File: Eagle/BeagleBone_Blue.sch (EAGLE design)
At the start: 294 parts, among them M1 JST_ZH_2, M2 JST_ZH_2, M3 JST_ZH_2, M4 JST_ZH_2, P10 SCHA5B0200, Q3 MOSFET-N, U1 TPD4S012_DRY_6, U4 TPD4S012_DRY_6, U5 24LC_32AT-I/OT, U6 SN74LVC1G07_DCK_5, U7 TPS2051B_D_8, U8 MTFC4GLDEA, Y1 CM200C-32.768KAZF-UT, Y2 445C33D24M00000

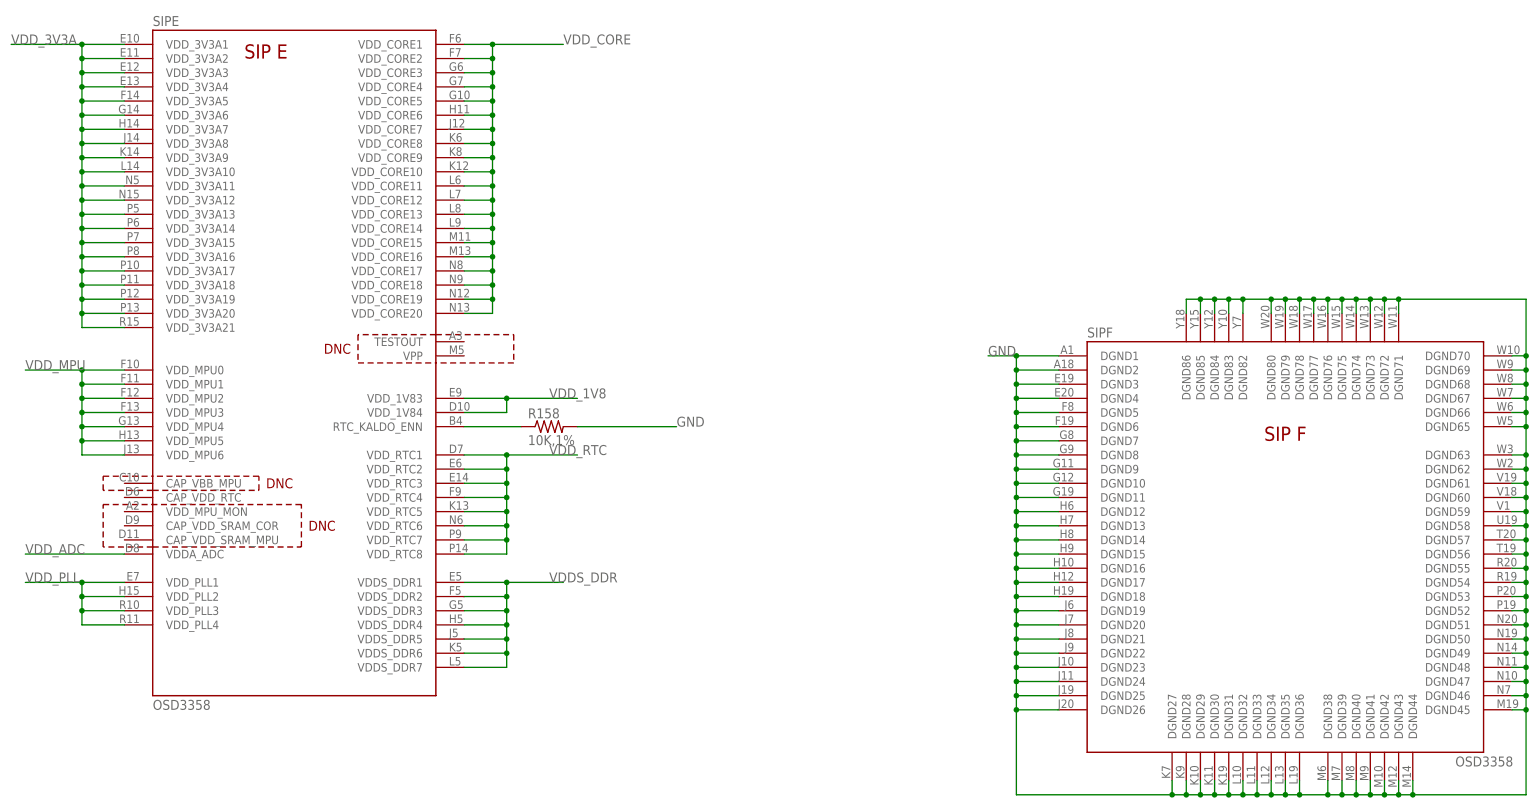
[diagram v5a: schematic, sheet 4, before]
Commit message: Remove extraneous voltage connections
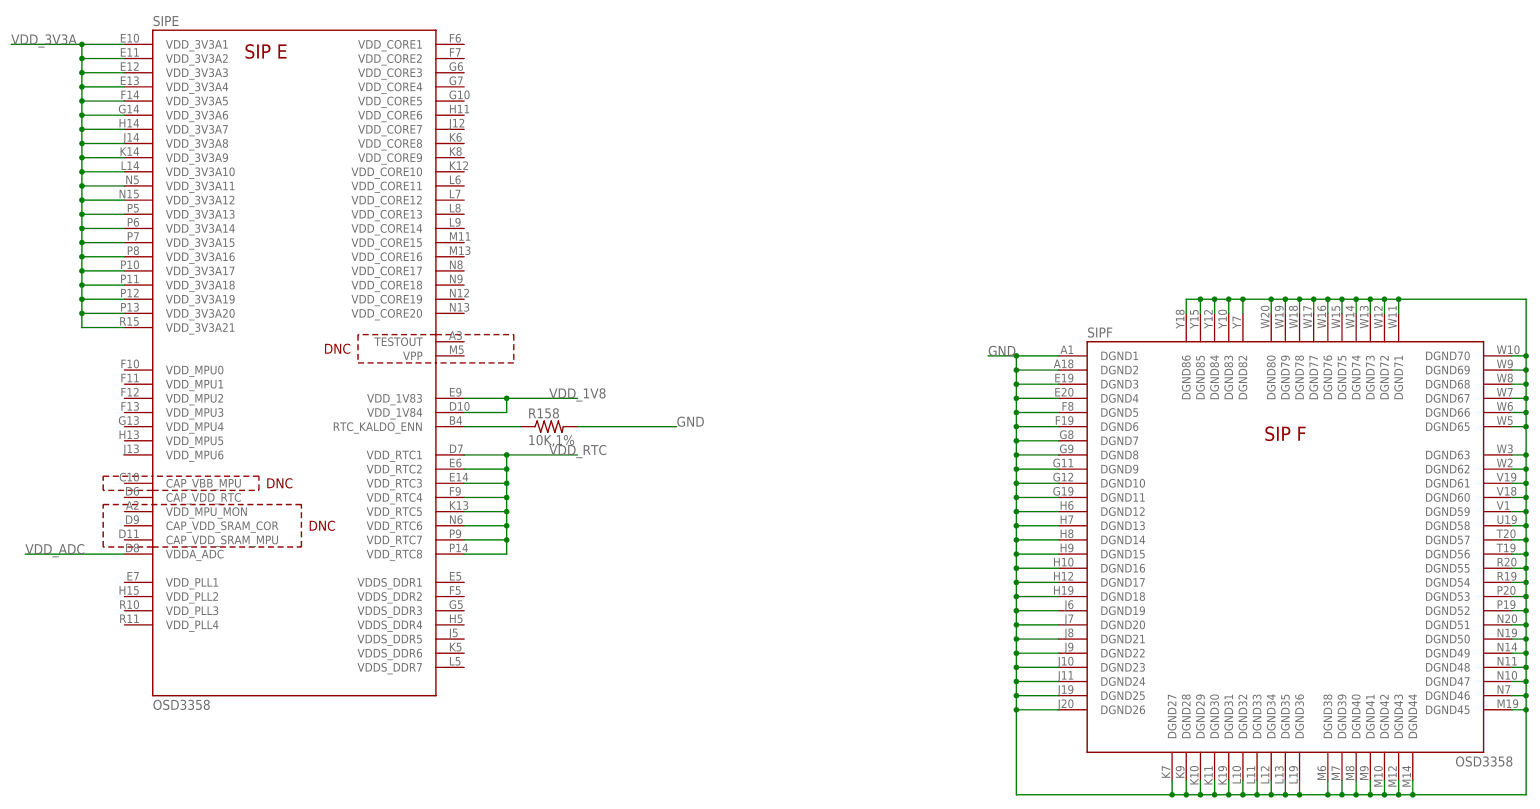
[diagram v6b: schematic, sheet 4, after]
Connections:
- removed net VDDS_DDR: SIPE.VDDS_DDR1, SIPE.VDDS_DDR2, SIPE.VDDS_DDR3, SIPE.VDDS_DDR4, SIPE.VDDS_DDR5, SIPE.VDDS_DDR6, SIPE.VDDS_DDR7
- removed net VDD_CORE: SIPE.VDD_CORE1, SIPE.VDD_CORE10, SIPE.VDD_CORE11, SIPE.VDD_CORE12, SIPE.VDD_CORE13, SIPE.VDD_CORE14, SIPE.VDD_CORE15, SIPE.VDD_CORE16, SIPE.VDD_CORE17, SIPE.VDD_CORE18, SIPE.VDD_CORE19, SIPE.VDD_CORE2, SIPE.VDD_CORE20, SIPE.VDD_CORE3, SIPE.VDD_CORE4, SIPE.VDD_CORE5, SIPE.VDD_CORE6, SIPE.VDD_CORE7, SIPE.VDD_CORE8, SIPE.VDD_CORE9
- removed net VDD_MPU: SIPE.VDD_MPU0, SIPE.VDD_MPU1, SIPE.VDD_MPU2, SIPE.VDD_MPU3, SIPE.VDD_MPU4, SIPE.VDD_MPU5, SIPE.VDD_MPU6
- removed net VDD_PLL: SIPE.VDD_PLL1, SIPE.VDD_PLL2, SIPE.VDD_PLL3, SIPE.VDD_PLL4
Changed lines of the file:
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@@
-</segment>
-</net>
-<net name="VDD_CORE" class="0">
-<segment>
-<pinref part="SIP" gate="E" pin="VDD_CORE1"/>
-<wire x1="134.62" y1="226.06" x2="139.7" y2="226.06" width="0.1524" layer="91"/>
-<pinref part="SIP" gate="E" pin="VDD_CORE2"/>
-<wire x1="139.7" y1="226.06" x2="152.4" y2="226.06" width="0.1524" layer="91"/>
-<wire x1="134.62" y1="223.52" x2="139.7" y2="223.52" width="0.1524" layer="91"/>
-<wire x1="139.7" y1="223.52" x2="139.7" y2="226.06" width="0.1524" layer="91"/>
-<junction x="139.7" y="226.06"/>
-<pinref part="SIP" gate="E" pin="VDD_CORE3"/>
-<wire x1="134.62" y1="220.98" x2="139.7" y2="220.98" width="0.1524" layer="91"/>
-<wire x1="139.7" y1="220.98" x2="139.7" y2="223.52" width="0.1524" layer="91"/>
-<junction x="139.7" y="223.52"/>
-<pinref part="SIP" gate="E" pin="VDD_CORE4"/>
-<wire x1="134.62" y1="218.44" x2="139.7" y2="218.44" width="0.1524" layer="91"/>
-<wire x1="139.7" y1="218.44" x2="139.7" y2="220.98" width="0.1524" layer="91"/>
-<junction x="139.7" y="220.98"/>
-<pinref part="SIP" gate="E" pin="VDD_CORE5"/>
-<wire x1="134.62" y1="215.9" x2="139.7" y2="215.9" width="0.1524" layer="91"/>
-<wire x1="139.7" y1="215.9" x2="139.7" y2="218.44" width="0.1524" layer="91"/>
-<junction x="139.7" y="218.44"/>
-<pinref part="SIP" gate="E" pin="VDD_CORE6"/>
-<wire x1="134.62" y1="213.36" x2="139.7" y2="213.36" width="0.1524" layer="91"/>
-<wire x1="139.7" y1="213.36" x2="139.7" y2="215.9" width="0.1524" layer="91"/>
-<junction x="139.7" y="215.9"/>
-<pinref part="SIP" gate="E" pin="VDD_CORE7"/>
-<wire x1="134.62" y1="210.82" x2="139.7" y2="210.82" width="0.1524" layer="91"/>
-<wire x1="139.7" y1="210.82" x2="139.7" y2="213.36" width="0.1524" layer="91"/>
-<junction x="139.7" y="213.36"/>
-<pinref part="SIP" gate="E" pin="VDD_CORE8"/>
-<wire x1="134.62" y1="208.28" x2="139.7" y2="208.28" width="0.1524" layer="91"/>
-<wire x1="139.7" y1="208.28" x2="139.7" y2="210.82" width="0.1524" layer="91"/>
-<junction x="139.7" y="210.82"/>
-<pinref part="SIP" gate="E" pin="VDD_CORE9"/>
-<wire x1="134.62" y1="205.74" x2="139.7" y2="205.74" width="0.1524" layer="91"/>
-<wire x1="139.7" y1="205.74" x2="139.7" y2="208.28" width="0.1524" layer="91"/>
-<junction x="139.7" y="208.28"/>
-<pinref part="SIP" gate="E" pin="VDD_CORE10"/>
-<wire x1="134.62" y1="203.2" x2="139.7" y2="203.2" width="0.1524" layer="91"/>
-<wire x1="139.7" y1="203.2" x2="139.7" y2="205.74" width="0.1524" layer="91"/>
-<junction x="139.7" y="205.74"/>
-<pinref part="SIP" gate="E" pin="VDD_CORE11"/>
-<wire x1="134.62" y1="200.66" x2="139.7" y2="200.66" width="0.1524" layer="91"/>
-<wire x1="139.7" y1="200.66" x2="139.7" y2="203.2" width="0.1524" layer="91"/>
-<junction x="139.7" y="203.2"/>
-<pinref part="SIP" gate="E" pin="VDD_CORE12"/>
-<wire x1="134.62" y1="198.12" x2="139.7" y2="198.12" width="0.1524" layer="91"/>
-<wire x1="139.7" y1="198.12" x2="139.7" y2="200.66" width="0.1524" layer="91"/>
-<junction x="139.7" y="200.66"/>
-<pinref part="SIP" gate="E" pin="VDD_CORE13"/>
-<wire x1="134.62" y1="195.58" x2="139.7" y2="195.58" width="0.1524" layer="91"/>
-<wire x1="139.7" y1="195.58" x2="139.7" y2="198.12" width="0.1524" layer="91"/>
-<junction x="139.7" y="198.12"/>
-<pinref part="SIP" gate="E" pin="VDD_CORE14"/>
-<wire x1="134.62" y1="193.04" x2="139.7" y2="193.04" width="0.1524" layer="91"/>
-<wire x1="139.7" y1="193.04" x2="139.7" y2="195.58" width="0.1524" layer="91"/>
-<junction x="139.7" y="195.58"/>
-<pinref part="SIP" gate="E" pin="VDD_CORE15"/>
-<wire x1="134.62" y1="190.5" x2="139.7" y2="190.5" width="0.1524" layer="91"/>
-<wire x1="139.7" y1="190.5" x2="139.7" y2="193.04" width="0.1524" layer="91"/>
-<junction x="139.7" y="193.04"/>
-<pinref part="SIP" gate="E" pin="VDD_CORE16"/>
-<wire x1="134.62" y1="187.96" x2="139.7" y2="187.96" width="0.1524" layer="91"/>
-<wire x1="139.7" y1="187.96" x2="139.7" y2="190.5" width="0.1524" layer="91"/>
-<junction x="139.7" y="190.5"/>
-<pinref part="SIP" gate="E" pin="VDD_CORE17"/>
-<wire x1="134.62" y1="185.42" x2="139.7" y2="185.42" width="0.1524" layer="91"/>
-<wire x1="139.7" y1="185.42" x2="139.7" y2="187.96" width="0.1524" layer="91"/>
-<junction x="139.7" y="187.96"/>
-<pinref part="SIP" gate="E" pin="VDD_CORE18"/>
-<wire x1="134.62" y1="182.88" x2="139.7" y2="182.88" width="0.1524" layer="91"/>
-<wire x1="139.7" y1="182.88" x2="139.7" y2="185.42" width="0.1524" layer="91"/>
-<junction x="139.7" y="185.42"/>
-<pinref part="SIP" gate="E" pin="VDD_CORE19"/>
-<wire x1="134.62" y1="180.34" x2="139.7" y2="180.34" width="0.1524" layer="91"/>
-<wire x1="139.7" y1="180.34" x2="139.7" y2="182.88" width="0.1524" layer="91"/>
-<junction x="139.7" y="182.88"/>
-<pinref part="SIP" gate="E" pin="VDD_CORE20"/>
-<wire x1="134.62" y1="177.8" x2="139.7" y2="177.8" width="0.1524" layer="91"/>
-<wire x1="139.7" y1="177.8" x2="139.7" y2="180.34" width="0.1524" layer="91"/>
-<junction x="139.7" y="180.34"/>
-<label x="152.4" y="226.06" size="1.778" layer="95"/>
-</segment>
-</net>
-<net name="VDD_MPU" class="0">
-<segment>
-<pinref part="SIP" gate="E" pin="VDD_MPU0"/>
-<wire x1="73.66" y1="167.64" x2="66.04" y2="167.64" width="0.1524" layer="91"/>
-<pinref part="SIP" gate="E" pin="VDD_MPU1"/>
-<wire x1="66.04" y1="167.64" x2="55.88" y2="167.64" width="0.1524" layer="91"/>
-<wire x1="73.66" y1="165.1" x2="66.04" y2="165.1" width="0.1524" layer="91"/>
-<wire x1="66.04" y1="165.1" x2="66.04" y2="167.64" width="0.1524" layer="91"/>
-<junction x="66.04" y="167.64"/>
-<pinref part="SIP" gate="E" pin="VDD_MPU2"/>
-<wire x1="73.66" y1="162.56" x2="66.04" y2="162.56" width="0.1524" layer="91"/>
-<wire x1="66.04" y1="162.56" x2="66.04" y2="165.1" width="0.1524" layer="91"/>
-<junction x="66.04" y="165.1"/>
-<pinref part="SIP" gate="E" pin="VDD_MPU3"/>
-<wire x1="73.66" y1="160.02" x2="66.04" y2="160.02" width="0.1524" layer="91"/>
-<wire x1="66.04" y1="160.02" x2="66.04" y2="162.56" width="0.1524" layer="91"/>
-<junction x="66.04" y="162.56"/>
-<pinref part="SIP" gate="E" pin="VDD_MPU4"/>
-<wire x1="73.66" y1="157.48" x2="66.04" y2="157.48" width="0.1524" layer="91"/>
-<wire x1="66.04" y1="157.48" x2="66.04" y2="160.02" width="0.1524" layer="91"/>
-<junction x="66.04" y="160.02"/>
-<pinref part="SIP" gate="E" pin="VDD_MPU5"/>
-<wire x1="73.66" y1="154.94" x2="66.04" y2="154.94" width="0.1524" layer="91"/>
-<wire x1="66.04" y1="154.94" x2="66.04" y2="157.48" width="0.1524" layer="91"/>
-<junction x="66.04" y="157.48"/>
-<pinref part="SIP" gate="E" pin="VDD_MPU6"/>
-<wire x1="73.66" y1="152.4" x2="66.04" y2="152.4" width="0.1524" layer="91"/>
-<wire x1="66.04" y1="152.4" x2="66.04" y2="154.94" width="0.1524" layer="91"/>
-<junction x="66.04" y="154.94"/>
-<label x="55.88" y="167.64" size="1.778" layer="95"/>
-</segment>
-</net>
-<net name="VDD_PLL" class="0">
-<segment>
-<pinref part="SIP" gate="E" pin="VDD_PLL1"/>
-<pinref part="SIP" gate="E" pin="VDD_PLL2"/>
-<wire x1="55.88" y1="129.54" x2="66.04" y2="129.54" width="0.1524" layer="91"/>
-<wire x1="66.04" y1="129.54" x2="73.66" y2="129.54" width="0.1524" layer="91"/>
-<wire x1="73.66" y1="127" x2="66.04" y2="127" width="0.1524" layer="91"/>
-<wire x1="66.04" y1="127" x2="66.04" y2="129.54" width="0.1524" layer="91"/>
-<junction x="66.04" y="129.54"/>
-<pinref part="SIP" gate="E" pin="VDD_PLL3"/>
-<wire x1="73.66" y1="124.46" x2="66.04" y2="124.46" width="0.1524" layer="91"/>
-<wire x1="66.04" y1="124.46" x2="66.04" y2="127" width="0.1524" layer="91"/>
-<junction x="66.04" y="127"/>
-<pinref part="SIP" gate="E" pin="VDD_PLL4"/>
-<wire x1="73.66" y1="121.92" x2="66.04" y2="121.92" width="0.1524" layer="91"/>
-<wire x1="66.04" y1="121.92" x2="66.04" y2="124.46" width="0.1524" layer="91"/>
-<junction x="66.04" y="124.46"/>
-<label x="55.88" y="129.54" size="1.778" layer="95"/>
 </segment>
 </net>
@@
 </segment>
 </net>
-<net name="VDDS_DDR" class="0">
-<segment>
-<pinref part="SIP" gate="E" pin="VDDS_DDR1"/>
-<wire x1="134.62" y1="129.54" x2="142.24" y2="129.54" width="0.1524" layer="91"/>
-<pinref part="SIP" gate="E" pin="VDDS_DDR2"/>
-<wire x1="142.24" y1="129.54" x2="152.4" y2="129.54" width="0.1524" layer="91"/>
-<wire x1="134.62" y1="127" x2="142.24" y2="127" width="0.1524" layer="91"/>
-<wire x1="142.24" y1="127" x2="142.24" y2="129.54" width="0.1524" layer="91"/>
-<junction x="142.24" y="129.54"/>
-<pinref part="SIP" gate="E" pin="VDDS_DDR3"/>
-<wire x1="134.62" y1="124.46" x2="142.24" y2="124.46" width="0.1524" layer="91"/>
-<wire x1="142.24" y1="124.46" x2="142.24" y2="127" width="0.1524" layer="91"/>
-<junction x="142.24" y="127"/>
-<pinref part="SIP" gate="E" pin="VDDS_DDR4"/>
-<wire x1="134.62" y1="121.92" x2="142.24" y2="121.92" width="0.1524" layer="91"/>
-<wire x1="142.24" y1="121.92" x2="142.24" y2="124.46" width="0.1524" layer="91"/>
-<junction x="142.24" y="124.46"/>
-<pinref part="SIP" gate="E" pin="VDDS_DDR5"/>
-<wire x1="134.62" y1="119.38" x2="142.24" y2="119.38" width="0.1524" layer="91"/>
-<wire x1="142.24" y1="119.38" x2="142.24" y2="121.92" width="0.1524" layer="91"/>
-<junction x="142.24" y="121.92"/>
-<pinref part="SIP" gate="E" pin="VDDS_DDR6"/>
-<wire x1="134.62" y1="116.84" x2="142.24" y2="116.84" width="0.1524" layer="91"/>
-<wire x1="142.24" y1="116.84" x2="142.24" y2="119.38" width="0.1524" layer="91"/>
-<junction x="142.24" y="119.38"/>
-<pinref part="SIP" gate="E" pin="VDDS_DDR7"/>
-<wire x1="134.62" y1="114.3" x2="142.24" y2="114.3" width="0.1524" layer="91"/>
-<wire x1="142.24" y1="114.3" x2="142.24" y2="116.84" width="0.1524" layer="91"/>
-<junction x="142.24" y="116.84"/>
-<label x="149.86" y="129.54" size="1.778" layer="95"/>
-</segment>
-</net>

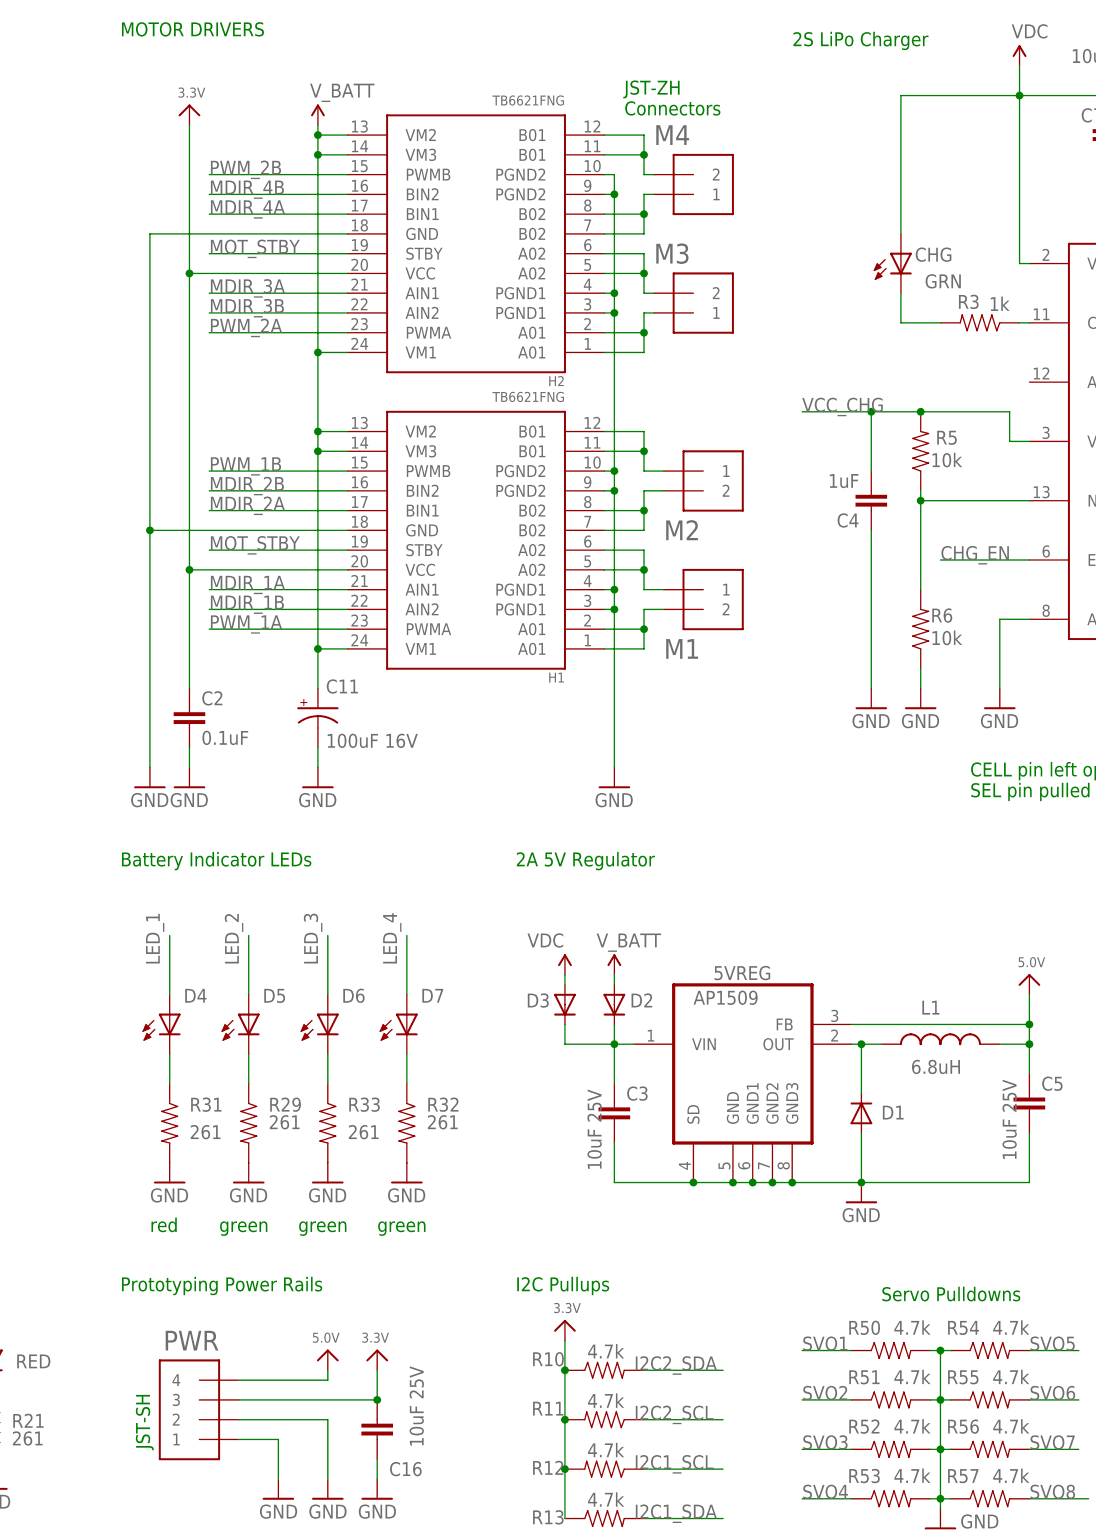
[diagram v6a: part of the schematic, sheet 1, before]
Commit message: Parts consistent but not nets
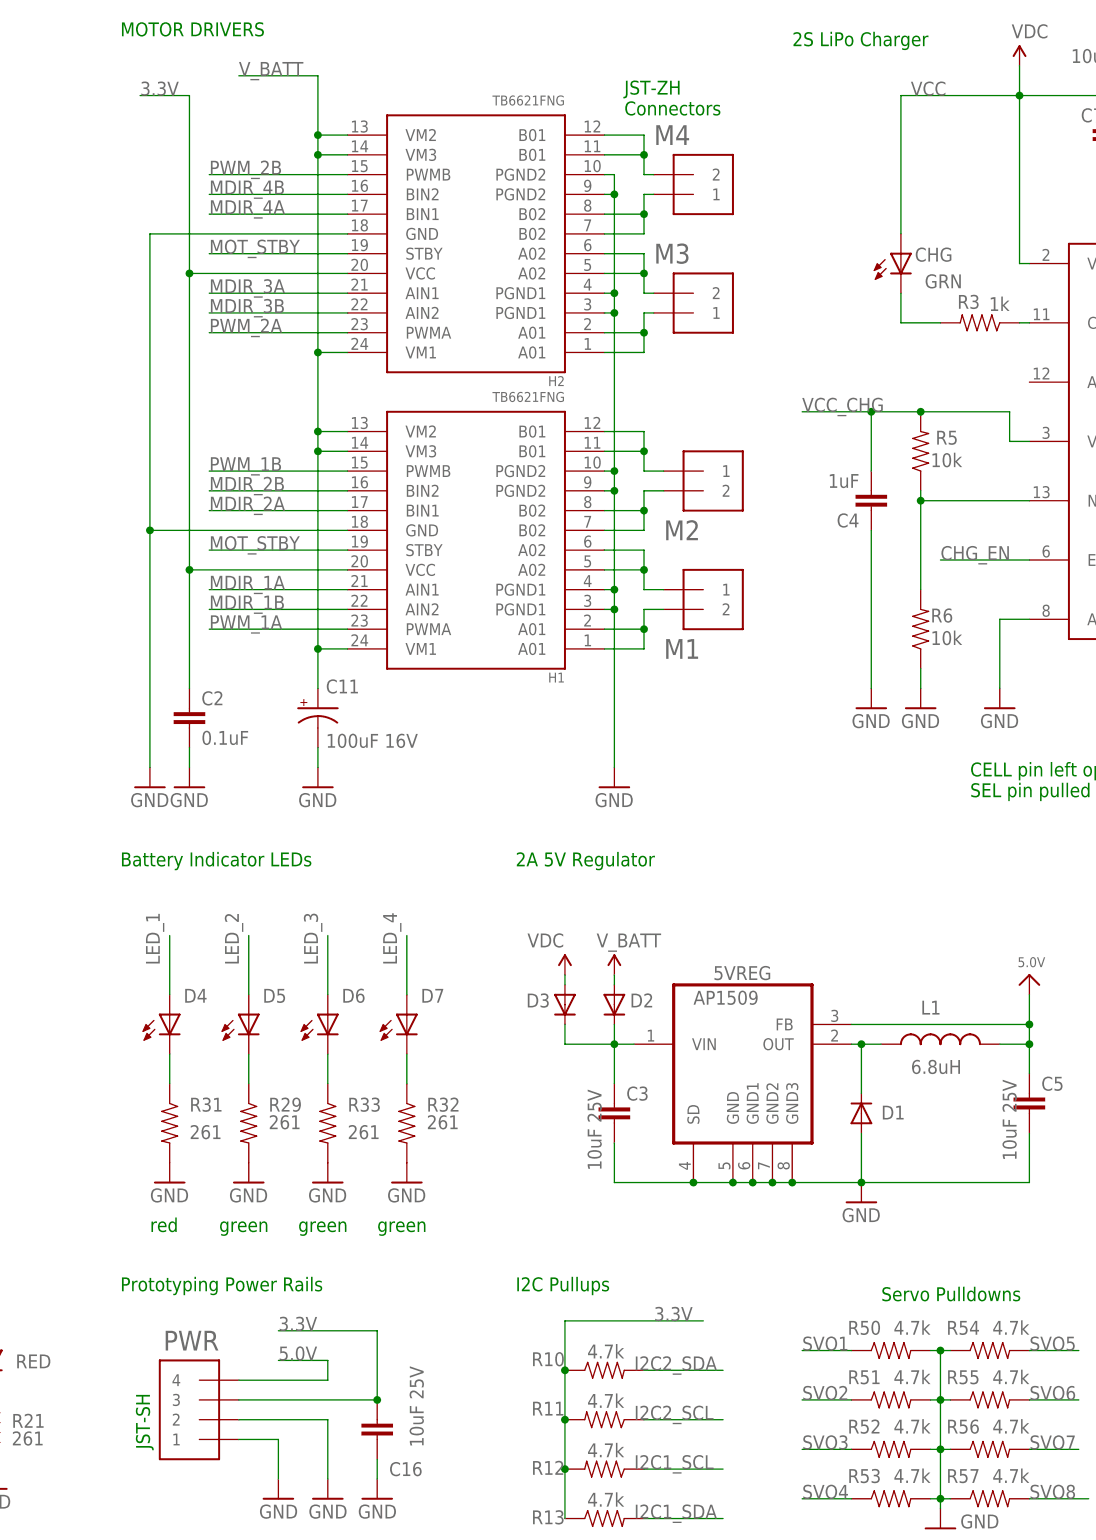
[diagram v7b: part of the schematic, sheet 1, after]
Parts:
- renumbered U$7 to C$1
